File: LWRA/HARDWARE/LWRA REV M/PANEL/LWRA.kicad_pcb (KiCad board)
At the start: 2 copper layers, 89.9 x 91.9 mm, 872 parts, among them P1 USB_OTG, P2 ICSP, SW1 Push_SW, U1 BMP280, U2 ATTINY841-MU, U3 FT230XQ-R

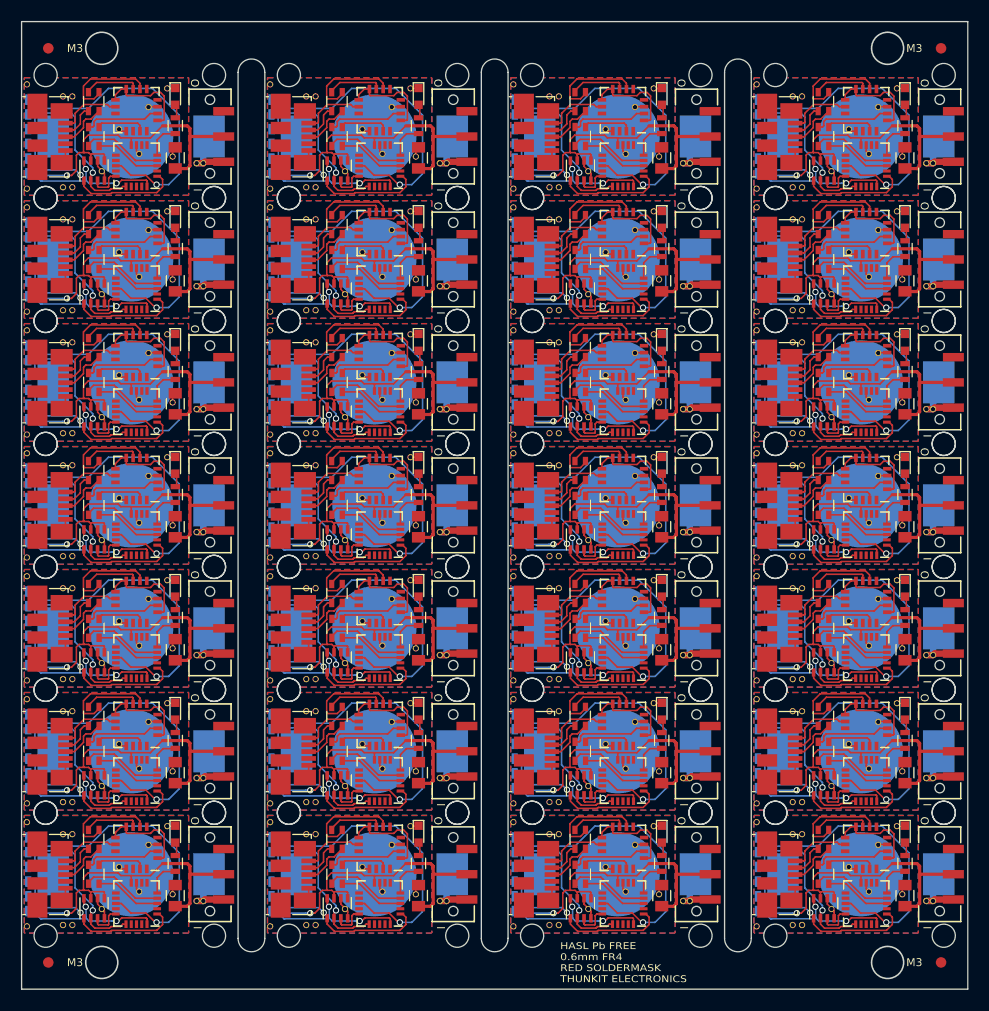
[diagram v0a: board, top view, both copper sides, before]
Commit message: fixed pin 1 dot on LWRA, firmware folder renamed
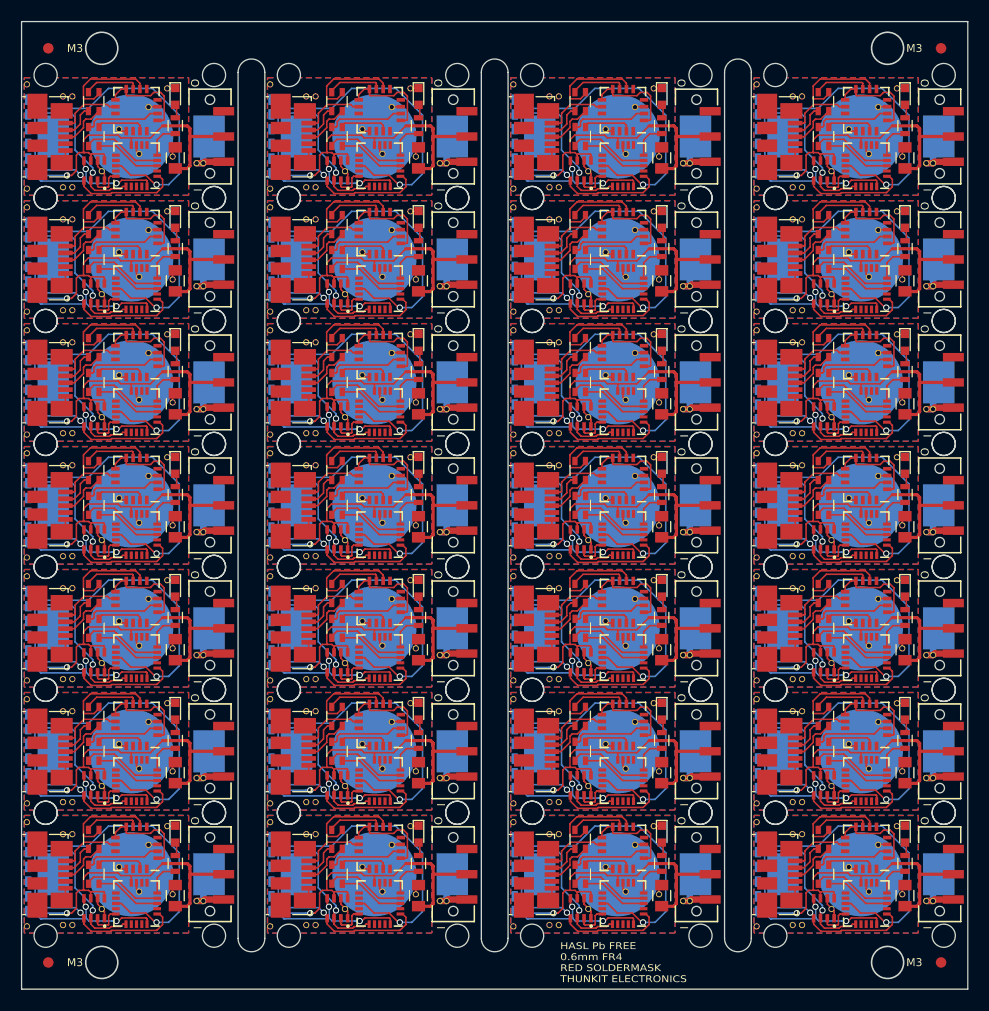
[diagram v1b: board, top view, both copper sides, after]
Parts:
- U1 (x28): footprint MOD:LGA-8_NO_DOT -> MOD:LGA-8_PIN1_DOT
